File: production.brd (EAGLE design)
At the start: 177.2 x 153.4 mm, 362 parts, among them IC1 LM2576, IC10 TUSB2046B, IC11 LM2576, IC12 LM50, IC13 LM50, IC14 74LS595D, IC15 74LS595D, IC16 VN5772AK, IC17 TUSB2046B, IC18 IC_FT230X-SSOP-16, IC19 LM50, IC2 74LS595D, IC20 LM50, IC21 VN5772AK, IC22 VN5772AK, IC23 VN5772AK, IC24 VN5772AK, IC3 74LS595D, IC4 IC_FT230X-SSOP-16, IC5 VN5772AK, IC6 VN5772AK, IC7 VN5772AK, IC8 VN5772AK, IC9 VN5772AK, U1 NCP4625, U2 NCP4625, U3 ATMEGA168, U4 ATMEGA168, Y1 16Mhz, Y2 6MHz, Y3 16Mhz, Y4 6MHz

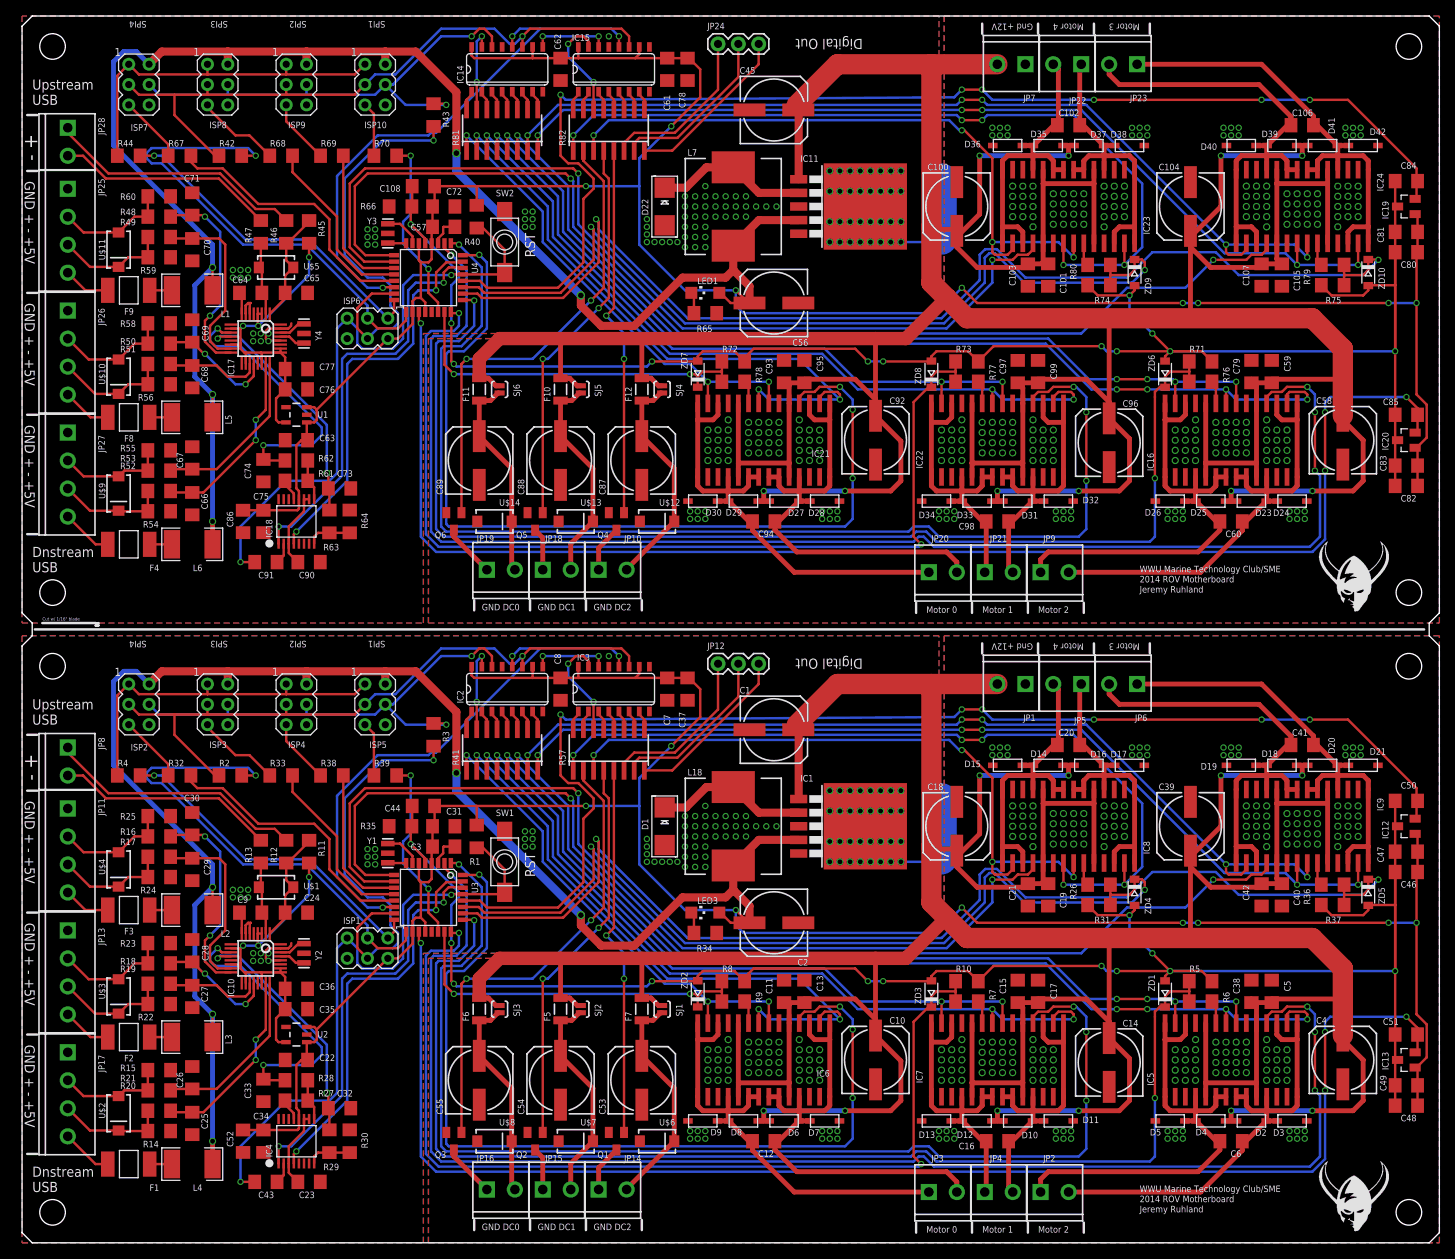
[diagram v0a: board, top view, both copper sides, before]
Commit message: added corrected motherboard to production board
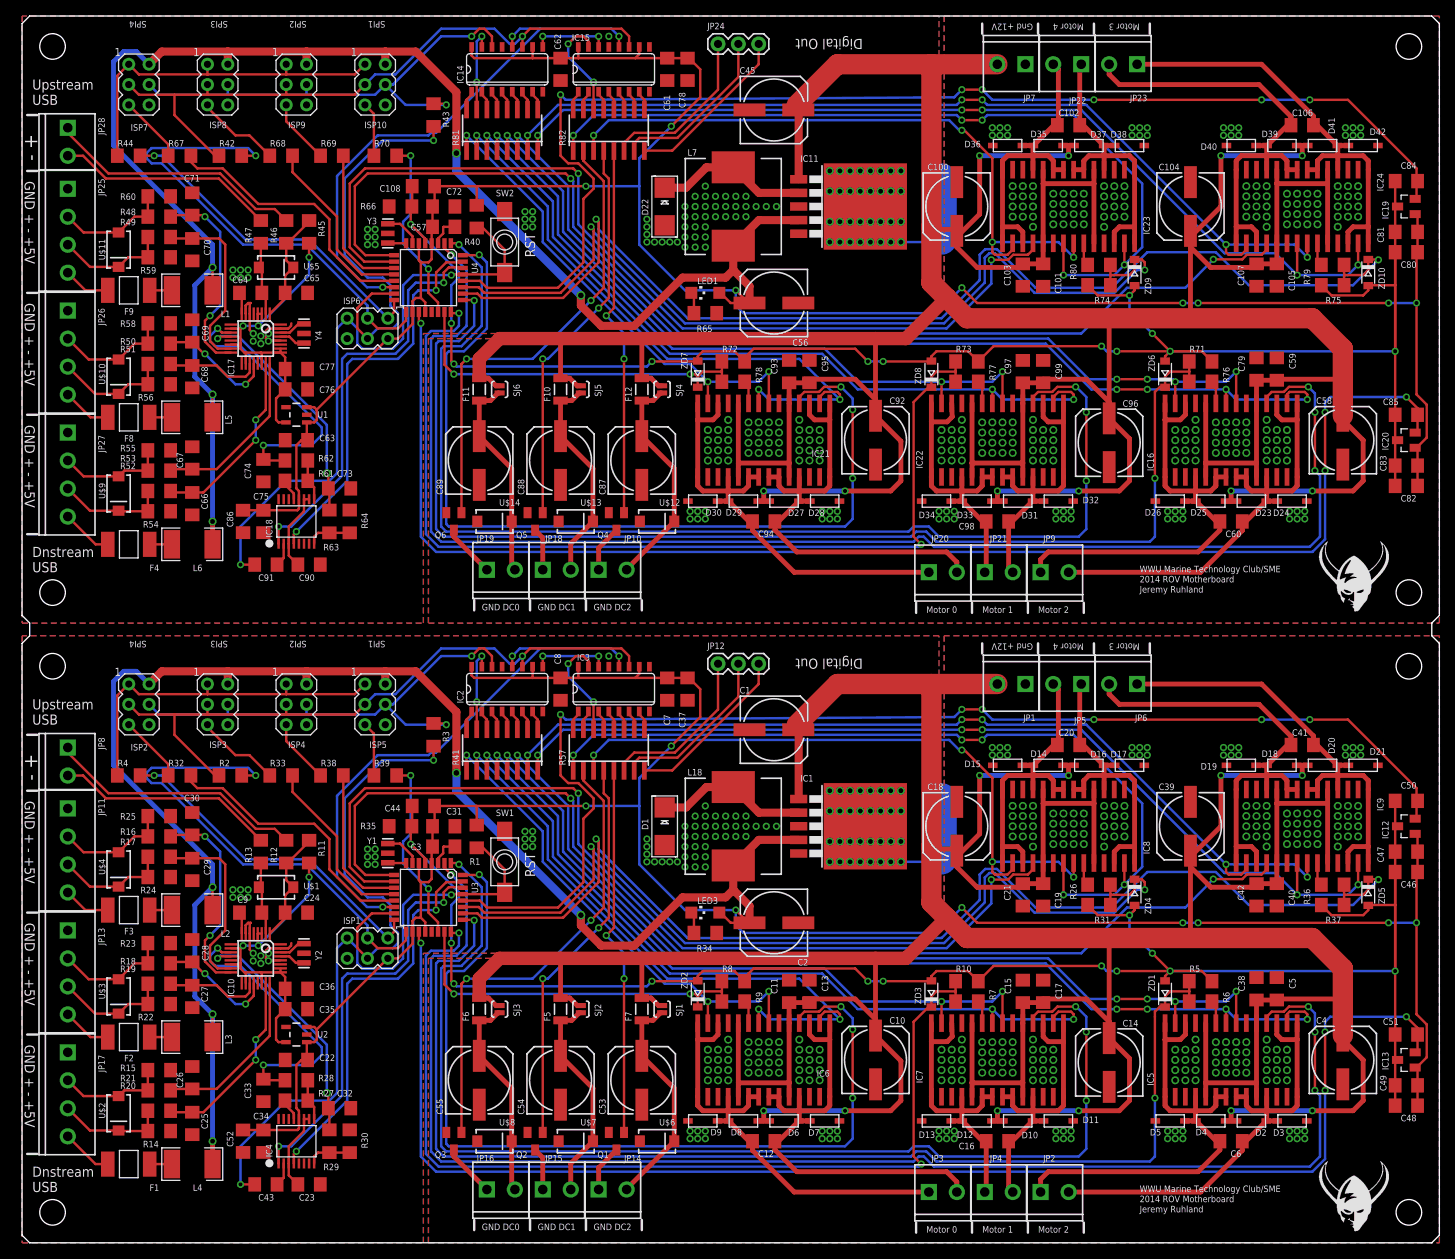
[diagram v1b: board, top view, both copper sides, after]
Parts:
- moved C38 0.71 mm to (154.3, 31.8)
- moved C79 0.71 mm to (154.3, 109.2)
- moved C5 0.71 mm to (156.8, 31.8)
- moved C59 0.71 mm to (156.8, 109.2)
- moved C101 0.64 mm to (127.6, 121.0)
- moved C103 0.64 mm to (125.1, 121.0)
- moved C11 0.64 mm to (95.9, 31.4)
- moved C15 0.64 mm to (125.1, 31.4)
- moved C17 0.64 mm to (127.6, 31.4)
- moved C19 0.64 mm to (127.6, 43.5)
- moved C21 0.64 mm to (125.1, 43.5)
- moved C93 0.64 mm to (95.9, 108.9)
- moved C97 0.64 mm to (125.1, 108.9)
- moved C99 0.64 mm to (127.6, 108.9)
- moved C105 0.63 mm to (156.8, 121.0)
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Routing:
- net GND: track 39.4 -> 42.0 mm, vias 369 -> 368
- net GND1: track 39.4 -> 42.0 mm, vias 369 -> 368
- net 3HB1: track 119.3 -> 121.6 mm
- net 3HB: track 119.3 -> 121.6 mm
- net 3SENSE1: track 146.7 -> 148.8 mm
- net 3SENSE: track 146.7 -> 148.8 mm
- net 2HB1: track 113.1 -> 114.9 mm
- net 1HB1: track 86.1 -> 87.9 mm
- net 4HB1: track 102.3 -> 104.1 mm
- net 2HB: track 113.1 -> 114.9 mm
- net 0HB1: track 60.1 -> 61.9 mm
- net 0HB: track 60.1 -> 61.9 mm
- net 4HB: track 102.3 -> 104.1 mm
- net 1HB: track 86.1 -> 87.9 mm
- net +12V1: track 623.9 -> 622.3 mm
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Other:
- outline, holes or cut-outs redrawn
- board text removed: "Cut w/ 1/16" blade"
